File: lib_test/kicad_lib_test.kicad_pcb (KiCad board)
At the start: 2 copper layers, 126 x 94 mm, 252 parts, among them Q6001 AO3400A, U7001 TLV272, U8001 LM335

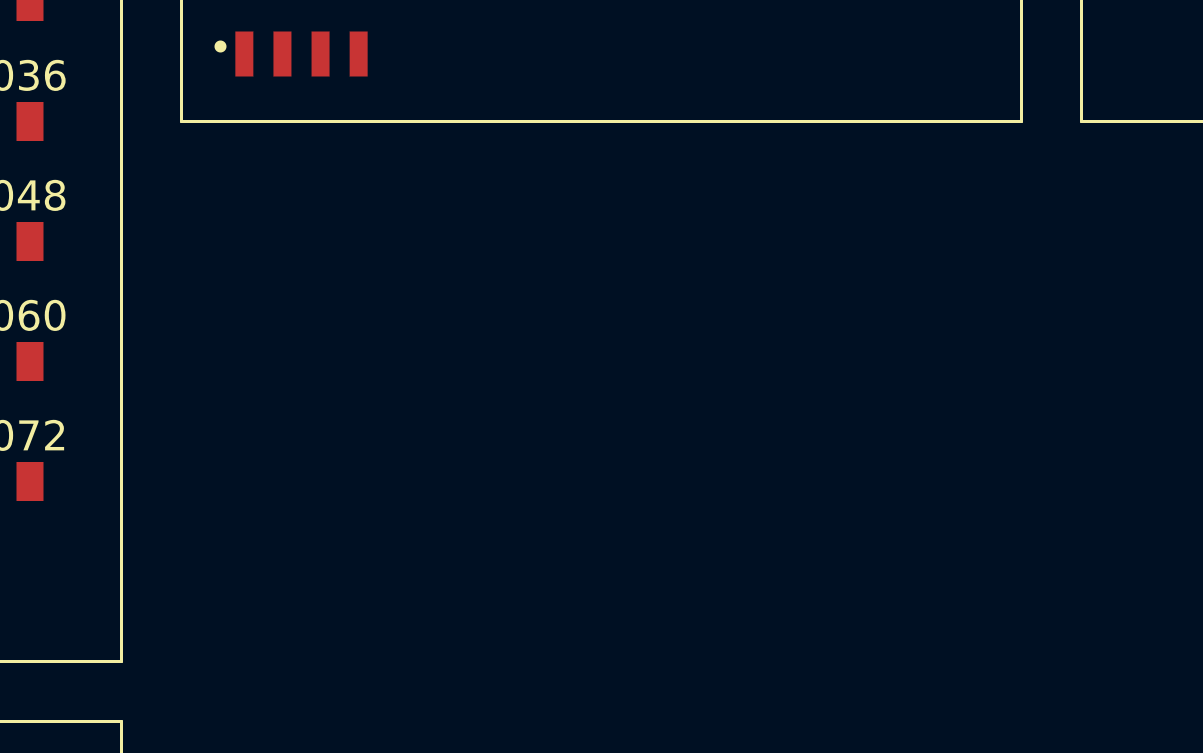
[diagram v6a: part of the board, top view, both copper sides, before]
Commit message: add LM393
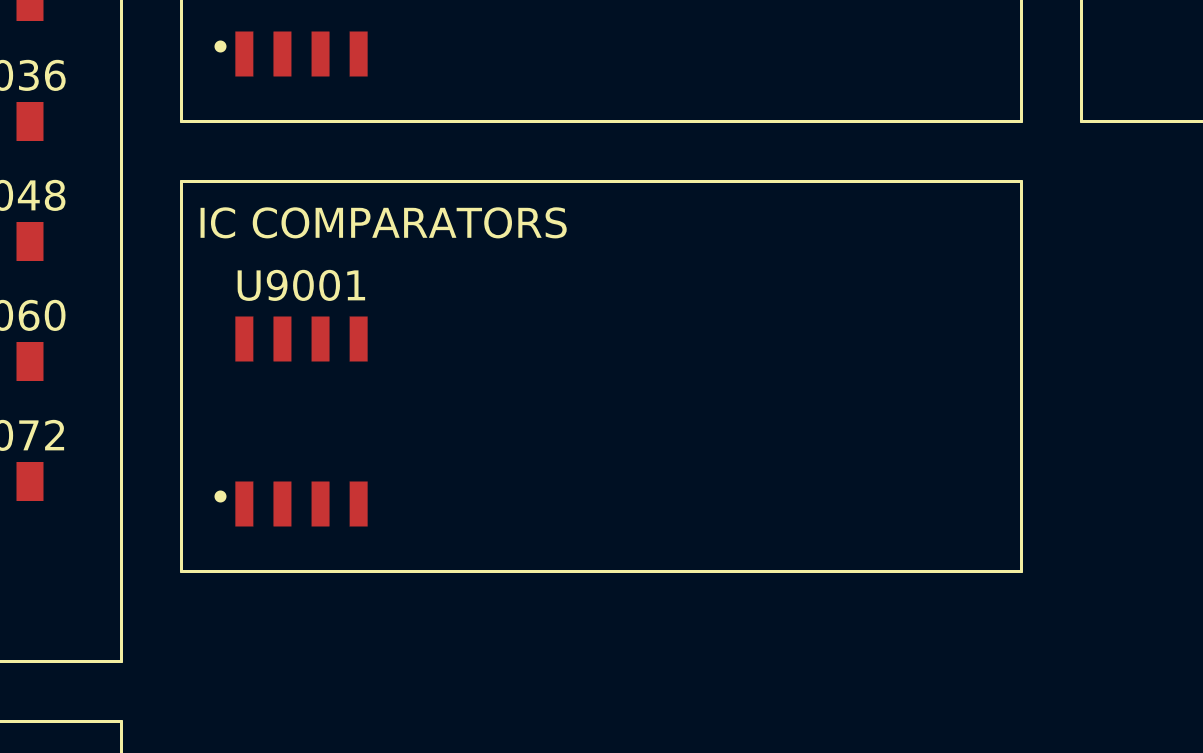
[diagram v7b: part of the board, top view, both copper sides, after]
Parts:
- added U9001: LM393, lily_footprints:soic8, F.Cu at (90.0, 82.0)
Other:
- board text added: "IC COMPARATORS"

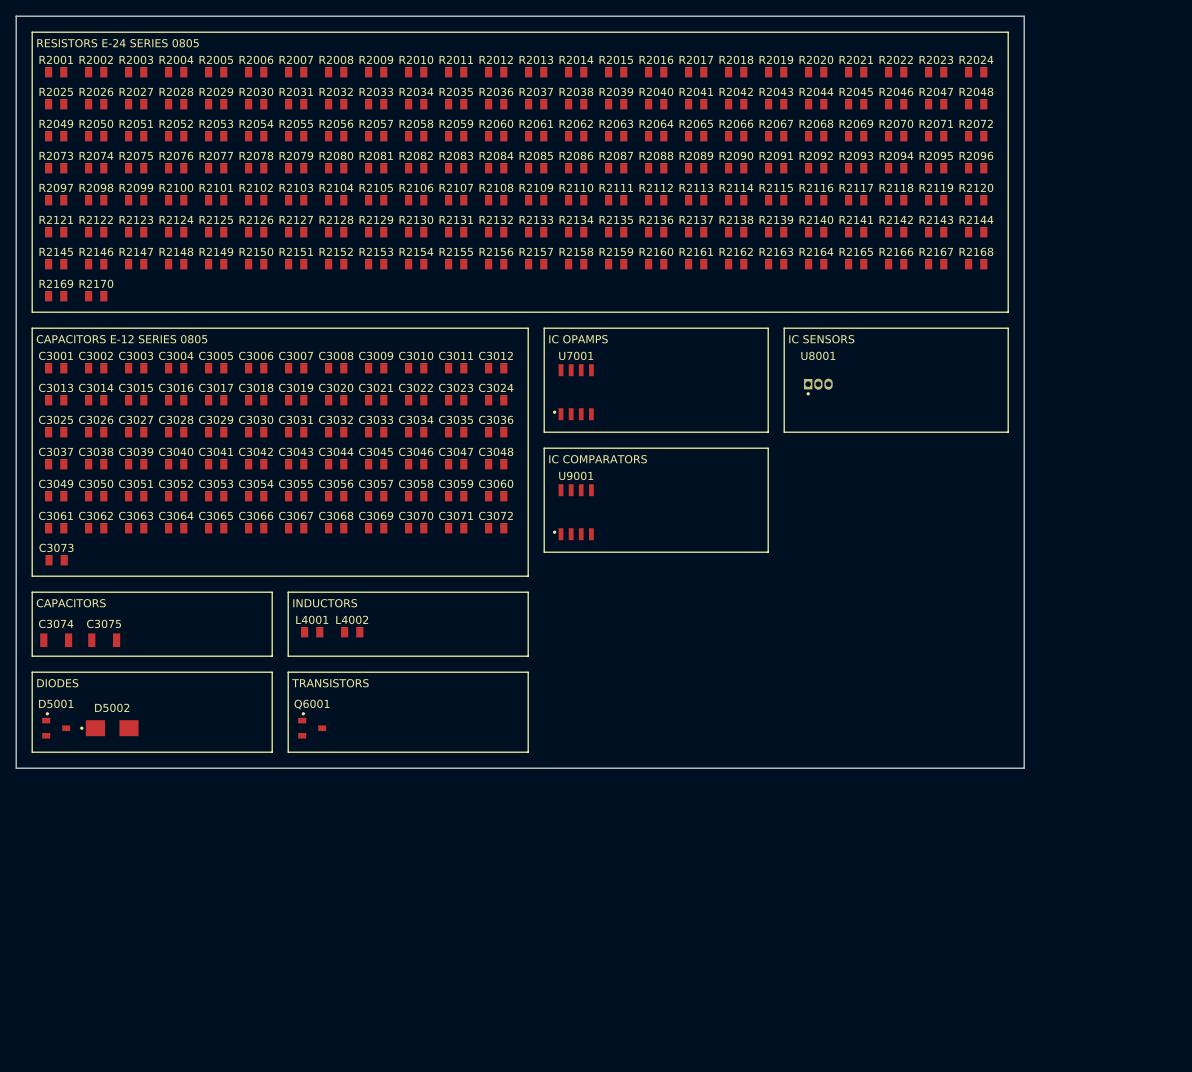
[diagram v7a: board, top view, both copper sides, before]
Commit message: add DIN41612 connector
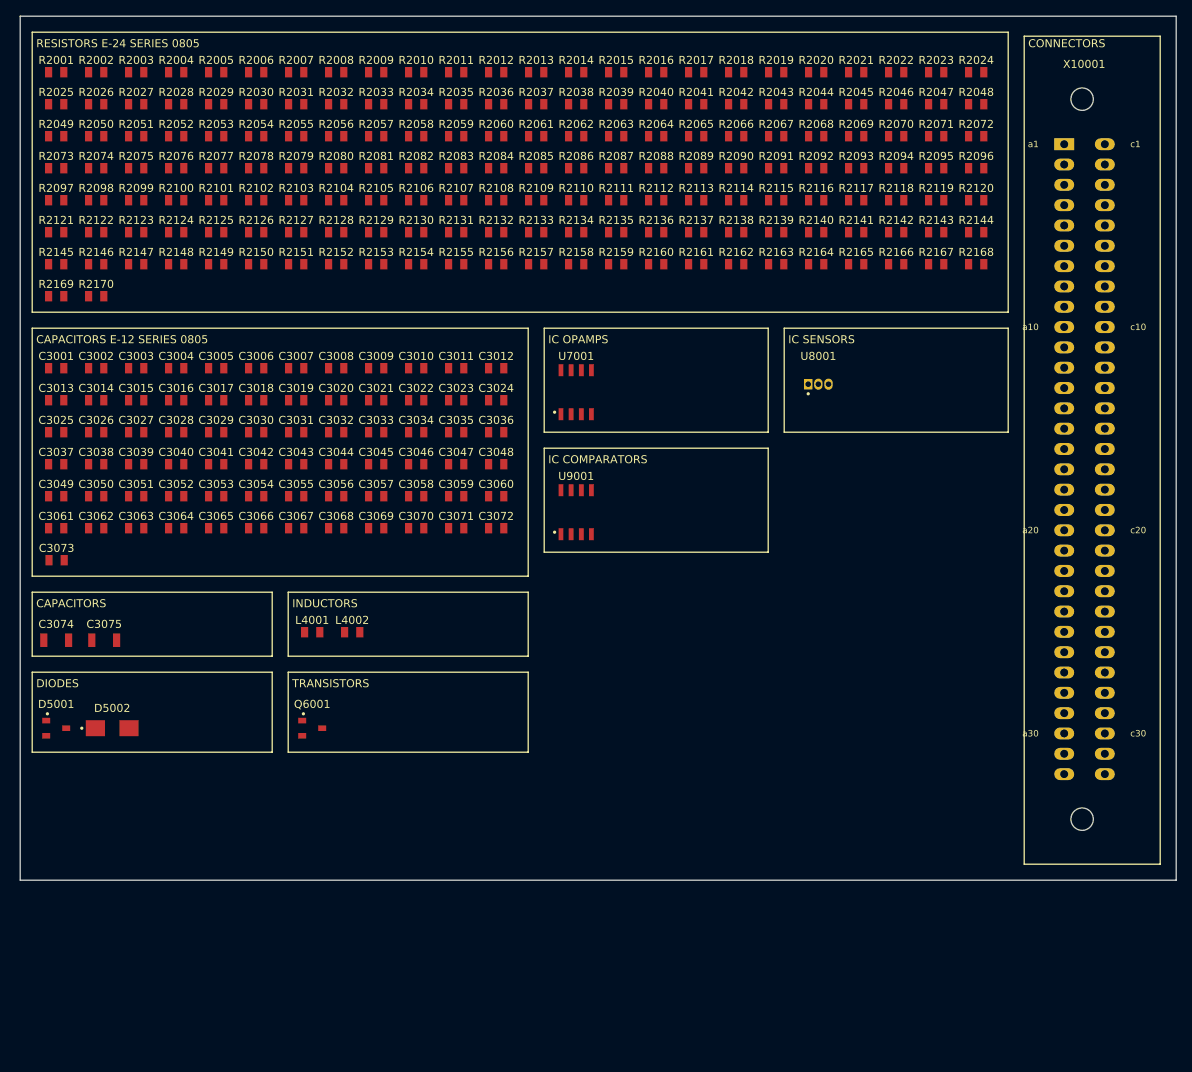
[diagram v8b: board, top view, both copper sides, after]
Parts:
- added X10001: con_din41612_receptacle_64p_a+c_straight_th, lily_footprints:con_din41612_receptacle_64p_a+c_straight_th, F.Cu at (151.0, 36.0)
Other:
- board size 126 x 94 mm -> 144.5 x 108 mm
- board text added: "CONNECTORS"
